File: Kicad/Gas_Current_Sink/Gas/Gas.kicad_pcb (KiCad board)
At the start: 2 copper layers, 17 parts, among them J1 MG811, J2 Digital, J3 MQ135, J4 CCS811, J5 Analog, J6 CONN_01X02, J7 CONN_01X02

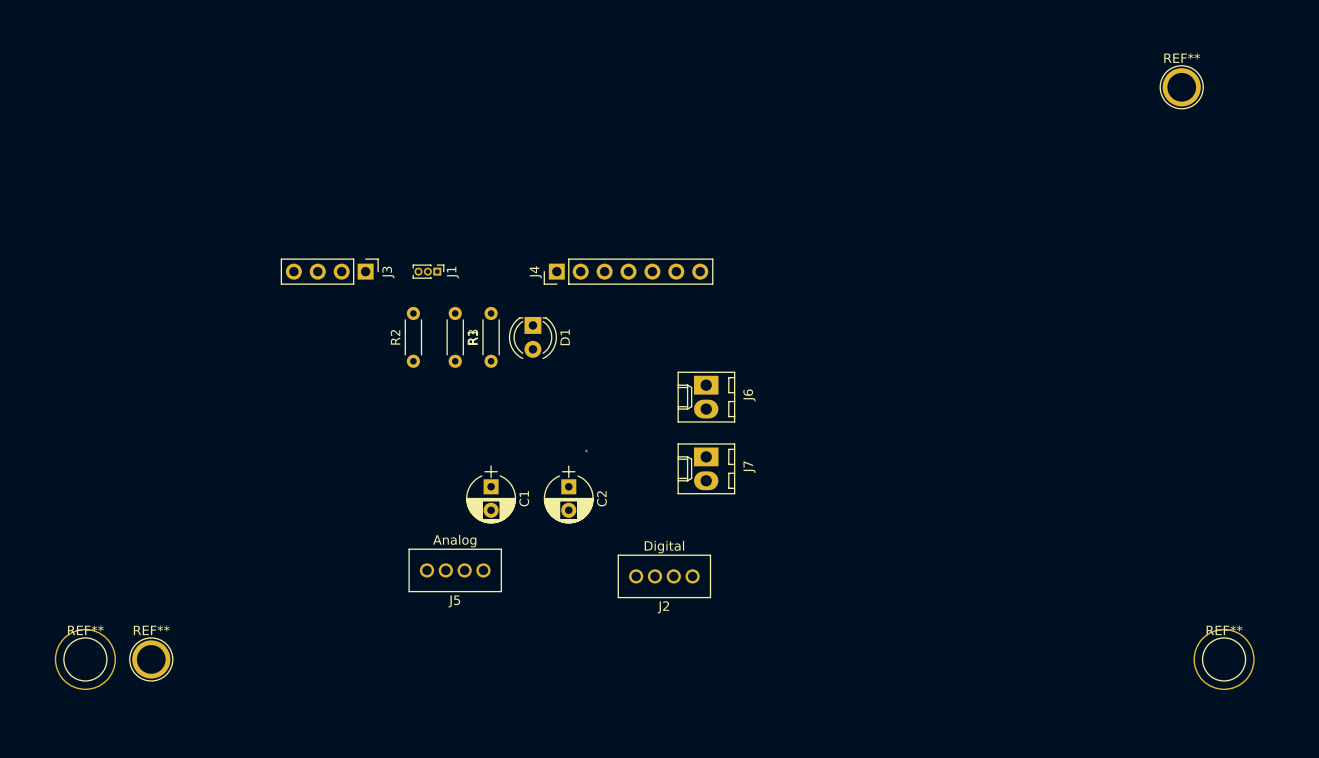
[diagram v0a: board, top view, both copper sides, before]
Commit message: @Kicad/Gas_Current_Sink/Gas: Finished PCB edge cutting and sensors placement project.
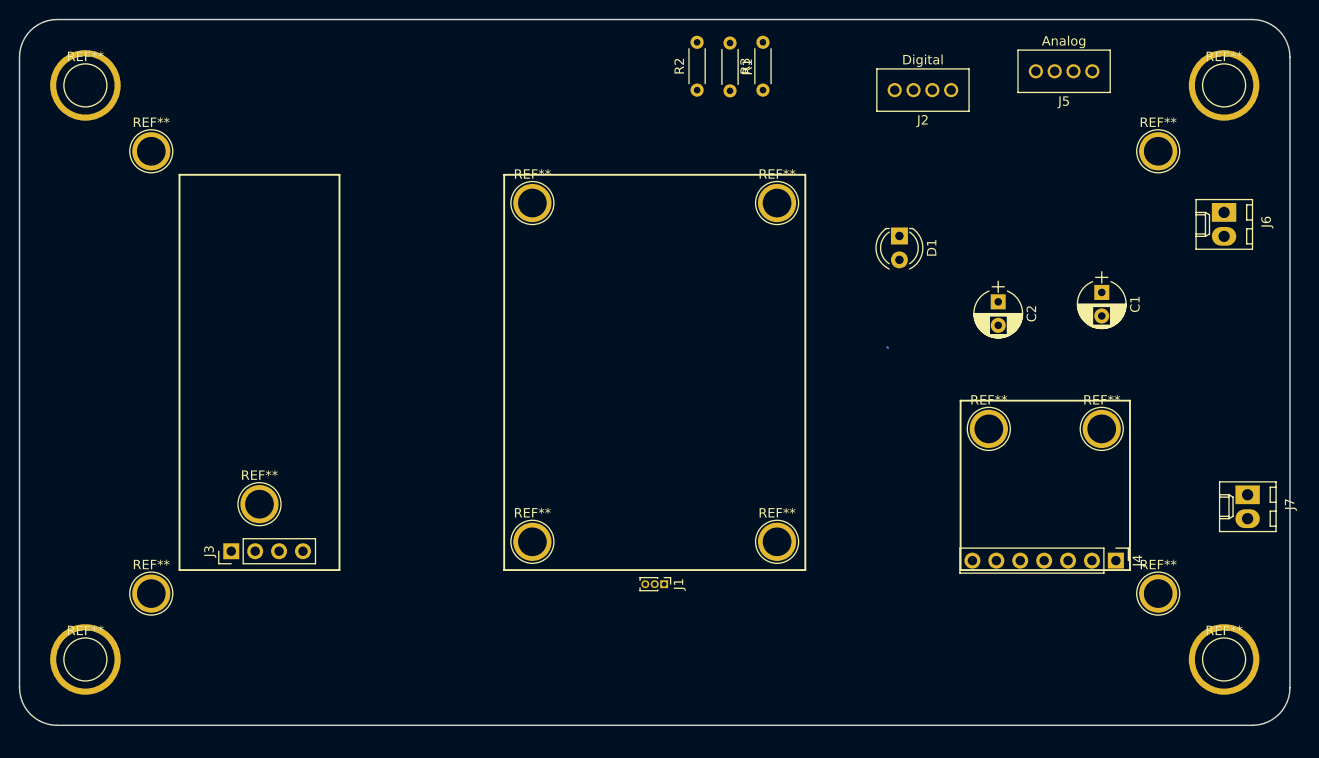
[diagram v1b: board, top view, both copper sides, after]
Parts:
- added REF**: 1pin, Connectors:1pin, F.Cu at (122.5, 126.5)
- added REF**: 1pin, Connectors:1pin, F.Cu at (148.5, 126.5)
- added REF**: 1pin, Connectors:1pin, F.Cu at (189.0, 85.0)
- added REF**: 1pin, Connectors:1pin, F.Cu at (189.0, 132.0)
- added REF**: 1pin, Connectors:1pin, F.Cu at (82.0, 132.0)
- added REF**: 1pin, Connectors:1pin, F.Cu at (82.0, 85.0)
- added REF**: 1pin, Connectors:1pin, F.Cu at (183.0, 114.5)
- added REF**: 1pin, Connectors:1pin, F.Cu at (93.5, 122.5)
- added REF**: 1pin, Connectors:1pin, F.Cu at (171.0, 114.5)
- added REF**: 1pin, Connectors:1pin, F.Cu at (148.5, 90.5)
- added REF**: 1pin, Connectors:1pin, F.Cu at (122.5, 90.5)
- moved J5 83.7 mm to (179.0, 76.5)
- moved C1 68.1 mm to (183.0, 100.0)
- moved J4 66.9 mm to (184.5, 128.5), turned to 270 degrees
- moved REF** 61.4 mm to (75.0, 78.0)
- moved J2 58.5 mm to (164.0, 78.5)
- moved J6 58.0 mm to (196.0, 91.5)
- moved J7 57.7 mm to (198.5, 121.5)
- moved C2 49.7 mm to (172.0, 101.0)
- moved R2 41.7 mm to (140.0, 78.5)
- moved J1 41.0 mm to (136.5, 131.0)
- moved R1 41.0 mm to (143.5, 73.5)
- moved R3 40.8 mm to (147.0, 78.5)
- moved D1 40.1 mm to (161.5, 94.0)
- moved J3 33.0 mm to (90.5, 127.5), turned to 90 degrees
- moved REF** 4.50 mm to (196.0, 78.0)
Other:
- board outline added: 135 x 75 mm

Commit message: Gas sensors PCB V1.00a
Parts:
- added D2: LED, LEDs:LED_D4.0mm, F.Cu at (139.5, 139.0)
- added G***: LOGO, ecoPlanos_custom:ecoplanos_logo_20mm, F.Cu at (178.0, 139.0)
- added R4: R, Resistors_THT:R_Axial_DIN0207_L6.3mm_D2.5mm_P7.62mm_Horizontal, F.Cu at (135.5, 143.0)
- added SHIELD401: ARDUINO_DUE_SHIELD, ecoPlanos_custom:ARDUINO_DUE_SHIELD_LAYOUT, F.Cu at (68.0, 144.0)
- J1: footprint Pin_Headers:Pin_Header_Straight_1x03_Pitch1.00mm -> Pin_Headers:Pin_Header_Straight_1x03_Pitch2.54mm
- J2, J5, J6, J7: moved to B.Cu
- R1, R2, R3: footprint Resistors_THT:R_Axial_DIN0204_L3.6mm_D1.6mm_P5.08mm_Horizontal -> Resistors_THT:R_Axial_DIN0207_L6.3mm_D2.5mm_P7.62mm_Horizontal
- moved J6 96.6 mm to (110.0, 135.5), turned to 0 degrees
- moved J3 84.0 mm to (174.5, 127.5)
- moved REF** 84.0 mm to (177.5, 122.5)
- moved J4 83.0 mm to (101.5, 128.5)
- moved REF** 83.0 mm to (100.0, 114.5)
- moved REF** 83.0 mm to (88.0, 114.5)
- moved J2 82.9 mm to (93.0, 121.2)
- moved C1 77.2 mm to (110.0, 125.0), turned to 0 degrees
- moved J5 65.6 mm to (150.2, 135.5), turned to 0 degrees
- moved R3 60.6 mm to (115.0, 130.0), turned to 180 degrees
- moved D1 55.5 mm to (129.0, 139.0), turned to 0 degrees
- moved R1 49.5 mm to (162.7, 119.1), turned to 90 degrees
- moved J7 39.6 mm to (161.5, 135.5), turned to 180 degrees
- moved R2 37.5 mm to (157.8, 111.5), turned to 270 degrees
- moved C2 26.2 mm to (161.5, 125.0), turned to 180 degrees
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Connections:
- net Net-(J3-Pad2) renamed /MQ135_out_5v
- J1 pad 3: Net-(J1-Pad3) -> /MG811_out
- J2 pad 1: (no net) -> /SDA
- J2 pad 2: /nRST -> /SCL
- J2 pad 3: /nINT -> /nWAKE
- J2 pad 4: /nWAKE -> /nINT
- J5 pad 1: /SCL -> Net-(J5-Pad1)
- J5 pad 2: /SDA -> /nRST
- J5 pad 3: Vout -> /MG811_out
- J5 pad 4: Net-(J1-Pad3) -> MQ135_out_3V3
- R1 pad 2: Vout -> MQ135_out_3V3
- R2 pad 1: Vout -> MQ135_out_3V3
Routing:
- net /nRST: track 0.00 -> 81.0 mm
- net GND: track 0.00 -> 74.9 mm, vias 0 -> 6
- net +3V3: track 0.00 -> 74.6 mm, vias 0 -> 4
- net MQ135_out_3V3: track 0.00 -> 38.5 mm, vias 0 -> 2
- net +5V: track 0.00 -> 36.7 mm, vias 0 -> 2
- net /MQ135_out_5v: track 0.00 -> 28.0 mm, vias 0 -> 2
- net Net-(D1-Pad2): track 0.00 -> 25.5 mm, vias 0 -> 2
- net /MG811_out: track 0.00 -> 17.2 mm, vias 0 -> 1
- net Net-(J5-Pad1): track 0.00 -> 12.0 mm, vias 0 -> 1
- net Net-(D2-Pad2): track 0.00 -> 10.5 mm, vias 0 -> 2
- net /nINT: track 0.00 -> 8.42 mm
- net /nWAKE: track 0.00 -> 7.75 mm
- net /SCL: track 0.00 -> 7.47 mm
- net /SDA: track 0.00 -> 7.42 mm
- added copper zone on F.Cu, net GND
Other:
- net class Default: trace_width 0.25 -> 1; via_dia 0.6 -> 1.25; via_drill 0.4 -> 0.5
- net class POWER added: clearance 0.5, trace_width 1.25, via_dia 1.75, via_drill 0.5
- rule pad_to_mask_clearance: 0.2 -> 0.25

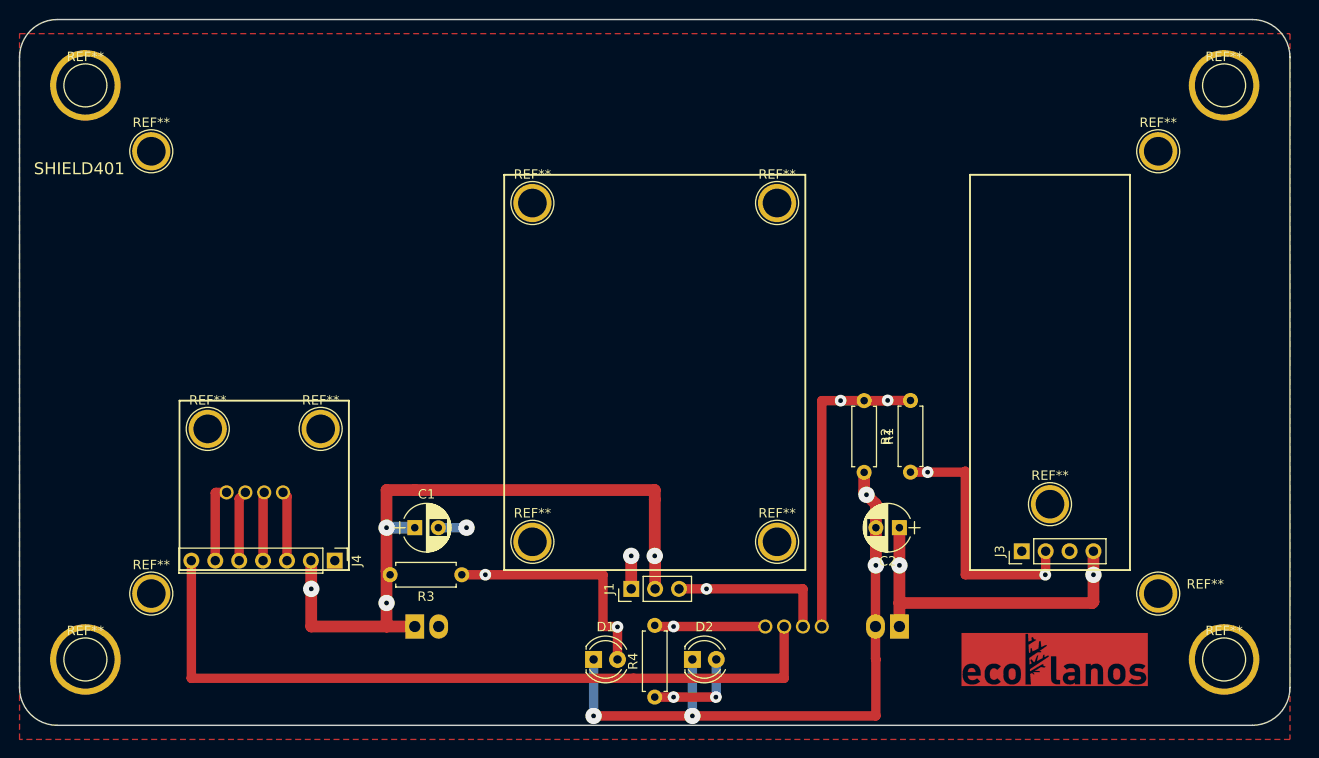
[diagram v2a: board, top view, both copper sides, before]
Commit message: @Gas_Current module - added kicad project for arduino due.
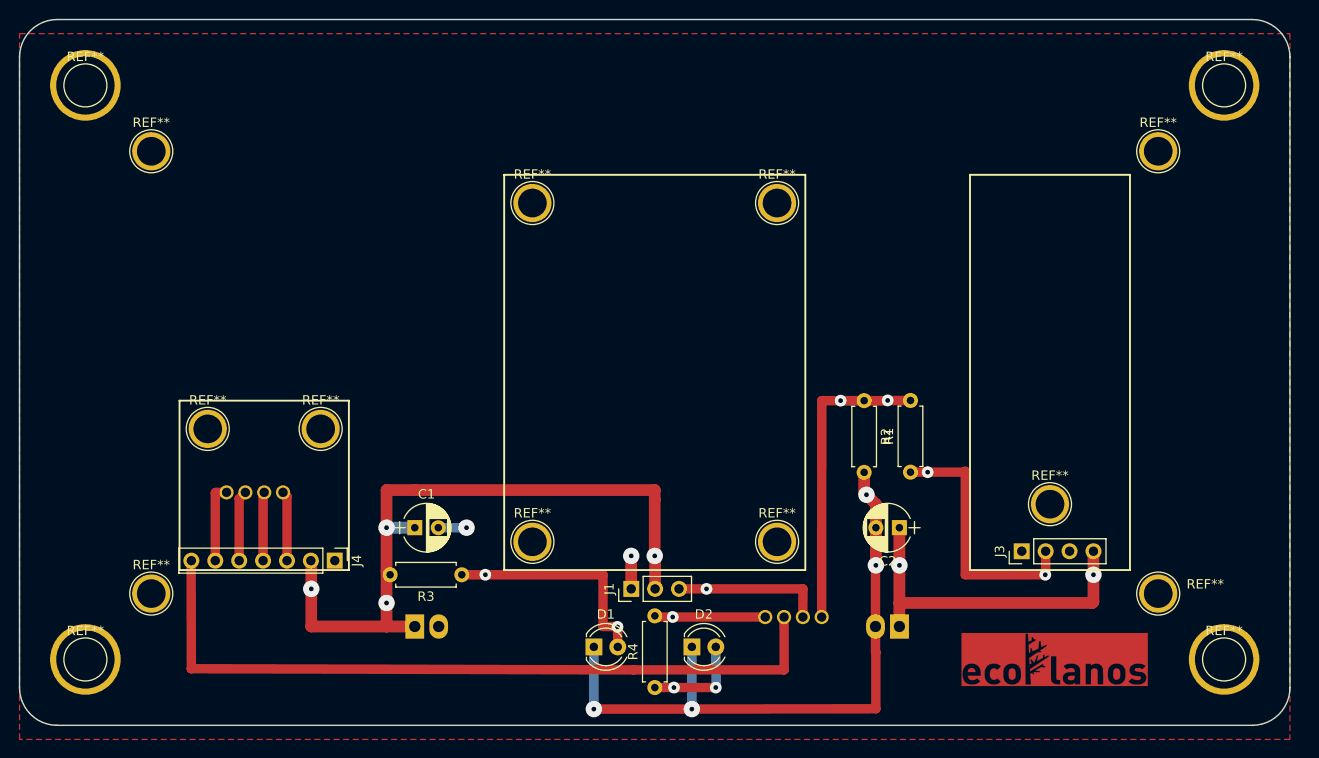
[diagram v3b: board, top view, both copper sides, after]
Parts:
- removed SHIELD401: ARDUINO_DUE_SHIELD, ecoPlanos_custom:ARDUINO_DUE_SHIELD_LAYOUT
- moved D2 1.33 mm to (139.4, 137.7)
- moved D1 1.33 mm to (129.0, 137.7)
- moved R4 1.01 mm to (135.5, 142.0)
- moved J5 1.01 mm to (150.2, 134.5)
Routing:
- net Net-(D1-Pad2): track 25.5 -> 24.2 mm
- net MQ135_out_3V3: track 38.5 -> 37.4 mm
- net /MG811_out: track 17.2 -> 16.2 mm
- net /nRST: track 81.0 -> 80.1 mm
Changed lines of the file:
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@@
-(kicad_pcb (version 4) (host pcbnew 4.0.7-e1-6374~58~ubuntu16.04.1)
+(kicad_pcb (version 4) (host pcbnew 4.0.7-e2-6376~58~ubuntu16.04.1)
   (general
     (links 27)
     (no_connects 0)
-    (area 67.924999 70.924999 203.075001 146.075001)
+    (area 44.650001 70.899999 217.85 156.700001)
     (thickness 1.6)
     (drawings 28)
     (tracks 115)
     (zones 0)
-    (modules 32)
+    (modules 31)
     (nets 15)
   )
@@
     (38 B.Mask user)
     (39 F.Mask user)
-    (40 Dwgs.User user hide)
-    (41 Cmts.User user hide)
+    (40 Dwgs.User user)
+    (41 Cmts.User user)
     (42 Eco1.User user)
     (43 Eco2.User user)
@@
   )
   (module LEDs:LED_D4.0mm locked (layer F.Cu)
-    (at 129 139)
+    (at 129.032 137.668)
     (descr "LED, diameter 4.0mm, 2 pins, http://www.kingbright.com/attachments/file/psearch/000/00/00/L-43GD(Ver.12B).pdf")
     (tags "LED diameter 4.0mm 2 pins")
@@
   )
   (module ecoPlanos_custom:JST_PHR-4 (layer B.Cu)
-    (at 150.25 135.5)
+    (at 150.241 134.493)
     (solder_mask_margin 0.1)
     (fp_text reference J5 (at 0 3.2) (layer B.SilkS)
@@
     (pad 1 thru_hole circle (at 0 0) (size 4.064 4.064) (drill 3.048) (layers *.Cu *.Mask))
   )
-  (module ecoPlanos_custom:ARDUINO_DUE_SHIELD_LAYOUT (layer F.Cu)
-    (at 68 144)
-    (descr http://www.thingiverse.com/thing:9630)
-    (fp_text reference SHIELD401 (at 6.35 -57.15) (layer F.SilkS)
-      (effects (font (thickness 0.3048)))
-    )
-    (fp_text value ARDUINO_DUE_SHIELD (at 13.97 -54.61) (layer F.SilkS) hide
-      (effects (font (thickness 0.3048)))
-    )
-    (fp_line (start 0 -12.7) (end 12.065 -12.7) (layer Cmts.User) (width 0.127))
-    (fp_line (start 12.065 -12.7) (end 12.065 0) (layer Cmts.User) (width 0.127))
-    (fp_line (start 99.06 0) (end 0 0) (layer Cmts.User) (width 0.381))
-    (fp_line (start 97.79 -53.34) (end 0 -53.34) (layer Cmts.User) (width 0.381))
-    (fp_line (start 99.06 -40.64) (end 99.06 -52.07) (layer Cmts.User) (width 0.381))
-    (fp_line (start 99.06 -52.07) (end 97.79 -53.34) (layer Cmts.User) (width 0.381))
-    (fp_line (start 0 0) (end 0 -53.34) (layer Cmts.User) (width 0.381))
-    (fp_line (start 99.06 -40.64) (end 101.6 -38.1) (layer Cmts.User) (width 0.381))
-    (fp_line (start 101.6 -38.1) (end 101.6 -5.08) (layer Cmts.User) (width 0.381))
-    (fp_line (start 101.6 -5.08) (end 99.06 -2.54) (layer Cmts.User) (width 0.381))
-    (fp_line (start 99.06 -2.54) (end 99.06 0) (layer Cmts.User) (width 0.381))
-    (model packages3d\nick\ArduinoMegaShield.wrl
-      (at (xyz 0 0 0))
-      (scale (xyz 1 1 1))
-      (rotate (xyz 0 0 0))
-    )
-  )
   (module LEDs:LED_D4.0mm locked (layer F.Cu)
-    (at 139.5 139)
+    (at 139.446 137.668)
     (descr "LED, diameter 4.0mm, 2 pins, http://www.kingbright.com/attachments/file/psearch/000/00/00/L-43GD(Ver.12B).pdf")
     (tags "LED diameter 4.0mm 2 pins")
@@
   )
   (module Resistors_THT:R_Axial_DIN0207_L6.3mm_D2.5mm_P7.62mm_Horizontal locked (layer F.Cu)
-    (at 135.5 143 90)
+    (at 135.509 141.986 90)
     (descr "Resistor, Axial_DIN0207 series, Axial, Horizontal, pin pitch=7.62mm, 0.25W = 1/4W, length*diameter=6.3*2.5mm^2, http://cdn-reichelt.de/documents/datenblatt/B400/1_4W%23YAG.pdf")
     (tags "Resistor Axial_DIN0207 series Axial Horizontal pin pitch 7.62mm 0.25W = 1/4W length 6.3mm diameter 2.5mm")
@@
   (segment (start 112.5 125) (end 115.5 125) (width 1) (layer B.Cu) (net 1))
   (via (at 115.5 125) (size 1.75) (drill 0.5) (layers F.Cu B.Cu) (net 1))
-  (segment (start 158.96 135.5) (end 158.96 138.96) (width 1) (layer F.Cu) (net 1))
-  (segment (start 159 145) (end 139.5 145) (width 1) (layer F.Cu) (net 1))
-  (segment (start 159 139) (end 159 145) (width 1) (layer F.Cu) (net 1))
-  (segment (start 158.96 138.96) (end 159 139) (width 1) (layer F.Cu) (net 1))
-  (segment (start 129 145) (end 129 139) (width 1) (layer B.Cu) (net 1))
-  (via (at 129 145) (size 1.75) (drill 0.5) (layers F.Cu B.Cu) (net 1))
-  (segment (start 139.5 145) (end 129 145) (width 1) (layer F.Cu) (net 1))
-  (via (at 139.5 145) (size 1.75) (drill 0.5) (layers F.Cu B.Cu) (net 1))
-  (segment (start 139.5 139) (end 139.5 145) (width 1) (layer B.Cu) (net 1))
+  (segment (start 158.96 135.5) (end 158.96 138.198) (width 1) (layer F.Cu) (net 1))
+  (segment (start 159 144.238) (end 139.446 144.272) (width 1) (layer F.Cu) (net 1))
+  (segment (start 159 138.238) (end 159 144.238) (width 1) (layer F.Cu) (net 1))
+  (segment (start 158.96 138.198) (end 159 138.238) (width 1) (layer F.Cu) (net 1))
+  (segment (start 129.032 144.272) (end 129.032 137.668) (width 1) (layer B.Cu) (net 1) (status 20))
+  (via (at 129.032 144.272) (size 1.75) (drill 0.5) (layers F.Cu B.Cu) (net 1))
+  (segment (start 139.446 144.272) (end 129.032 144.272) (width 1) (layer F.Cu) (net 1))
+  (via (at 139.446 144.272) (size 1.75) (drill 0.5) (layers F.Cu B.Cu) (net 1))
+  (segment (start 139.446 137.668) (end 139.446 144.272) (width 1) (layer B.Cu) (net 1) (status 10))
   (via (at 182.12 130) (size 1.75) (drill 0.5) (layers F.Cu B.Cu) (net 2))
   (segment (start 182.12 130) (end 182 130) (width 1.25) (layer B.Cu) (net 2))
@@
   (via (at 131.54 135.54) (size 1.25) (drill 0.5) (layers F.Cu B.Cu) (net 4))
   (segment (start 131.54 135.54) (end 131.5 135.5) (width 1) (layer B.Cu) (net 4))
-  (segment (start 131.54 139) (end 131.54 135.54) (width 1) (layer F.Cu) (net 4))
+  (segment (start 131.572 137.668) (end 131.54 135.54) (width 1) (layer F.Cu) (net 4) (status 10))
   (segment (start 130 135.5) (end 131.5 135.5) (width 1) (layer F.Cu) (net 4))
   (segment (start 130 130) (end 130 135.5) (width 1) (layer F.Cu) (net 4))
@@
   (segment (start 88.85 121.25) (end 90 121.25) (width 1) (layer F.Cu) (net 8))
   (segment (start 88.8 121.3) (end 88.85 121.25) (width 1) (layer F.Cu) (net 8))
-  (segment (start 133.25 141) (end 86.25 141) (width 1) (layer F.Cu) (net 9))
-  (segment (start 149.25 141) (end 133.25 141) (width 1) (layer F.Cu) (net 9))
-  (segment (start 149.25 135.5) (end 149.25 141) (width 1) (layer F.Cu) (net 9))
-  (segment (start 86.26 140.99) (end 86.26 128.5) (width 1) (layer F.Cu) (net 9))
-  (segment (start 86.25 141) (end 86.26 140.99) (width 1) (layer F.Cu) (net 9))
-  (segment (start 135.5 143) (end 137.5 143) (width 1) (layer F.Cu) (net 10))
-  (via (at 137.5 143) (size 1.25) (drill 0.5) (layers F.Cu B.Cu) (net 10))
-  (segment (start 137.5 143) (end 142 143) (width 1) (layer F.Cu) (net 10))
-  (via (at 142 143) (size 1.25) (drill 0.5) (layers F.Cu B.Cu) (net 10))
-  (segment (start 142 143) (end 142.04 142.96) (width 1) (layer B.Cu) (net 10))
-  (segment (start 142.04 142.96) (end 142.04 139) (width 1) (layer B.Cu) (net 10))
-  (segment (start 137.5 135.5) (end 135.62 135.5) (width 1) (layer F.Cu) (net 11))
-  (segment (start 135.62 135.5) (end 135.5 135.38) (width 1) (layer F.Cu) (net 11))
-  (segment (start 137.5 135.5) (end 147.25 135.5) (width 1) (layer F.Cu) (net 11) (status 20))
-  (via (at 137.5 135.5) (size 1.25) (drill 0.5) (layers F.Cu B.Cu) (net 11))
-  (segment (start 137.38 135.38) (end 137.5 135.5) (width 1) (layer B.Cu) (net 11))
+  (segment (start 133.25 140.111) (end 86.25 139.984) (width 1) (layer F.Cu) (net 9))
+  (segment (start 149.25 140.111) (end 133.25 140.111) (width 1) (layer F.Cu) (net 9))
+  (segment (start 149.241 134.493) (end 149.25 140.111) (width 1) (layer F.Cu) (net 9) (status 10))
+  (segment (start 86.26 139.974) (end 86.233 128.524) (width 1) (layer F.Cu) (net 9))
+  (segment (start 86.25 139.984) (end 86.26 139.974) (width 1) (layer F.Cu) (net 9))
+  (segment (start 135.509 141.986) (end 137.541 141.986) (width 1) (layer F.Cu) (net 10) (status 10))
+  (via (at 137.541 141.986) (size 1.25) (drill 0.5) (layers F.Cu B.Cu) (net 10))
+  (segment (start 137.541 141.986) (end 141.986 141.986) (width 1) (layer F.Cu) (net 10))
+  (via (at 141.986 141.986) (size 1.25) (drill 0.5) (layers F.Cu B.Cu) (net 10))
+  (segment (start 141.986 141.986) (end 142.026 141.946) (width 1) (layer B.Cu) (net 10))
+  (segment (start 142.026 141.946) (end 141.986 137.668) (width 1) (layer B.Cu) (net 10) (status 20))
+  (segment (start 137.414 134.493) (end 135.629 134.486) (width 1) (layer F.Cu) (net 11) (status 20))
+  (segment (start 135.629 134.486) (end 135.509 134.366) (width 1) (layer F.Cu) (net 11) (status 30))
+  (segment (start 137.414 134.493) (end 147.241 134.493) (width 1) (layer F.Cu) (net 11) (status 20))
+  (via (at 137.414 134.493) (size 1.25) (drill 0.5) (layers F.Cu B.Cu) (net 11))
+  (segment (start 137.294 134.373) (end 137.414 134.493) (width 1) (layer B.Cu) (net 11))
   (segment (start 138.08 131.5) (end 141 131.5) (width 1) (layer F.Cu) (net 12))
   (via (at 141 131.5) (size 1.25) (drill 0.5) (layers F.Cu B.Cu) (net 12))
   (segment (start 151.25 131.5) (end 141 131.5) (width 1) (layer F.Cu) (net 12))
-  (segment (start 151.25 131.5) (end 151.25 135.5) (width 1) (layer F.Cu) (net 12))
+  (segment (start 151.25 131.5) (end 151.241 134.493) (width 1) (layer F.Cu) (net 12) (status 20))
   (via (at 164.5 119.1) (size 1.25) (drill 0.5) (layers F.Cu B.Cu) (net 13))
   (segment (start 164.5 119.1) (end 164.5 119) (width 1) (layer B.Cu) (net 13))
@@
   (via (at 160.25 111.475) (size 1.25) (drill 0.5) (layers F.Cu B.Cu) (net 14))
   (segment (start 160.255 111.48) (end 160.25 111.475) (width 1) (layer B.Cu) (net 14))
-  (segment (start 153.25 135.5) (end 153.25 111.5) (width 1) (layer F.Cu) (net 14))
+  (segment (start 153.241 134.493) (end 153.25 111.5) (width 1) (layer F.Cu) (net 14) (status 10))
   (segment (start 153.25 111.5) (end 155.25 111.5) (width 1) (layer F.Cu) (net 14))
   (zone (net 1) (net_name GND) (layer F.Cu) (hatch edge 0.508)
